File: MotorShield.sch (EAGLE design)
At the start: 127 parts, among them IC1 OPA4340E, IC2 OPA4340E, IC3 74HCT125D, IC4 MCP3008SL, T1 FDN337N, T2 FDN337N, T3 FDN337N, T4 FDN337N, T5 FDN337N, T6 FDN337N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

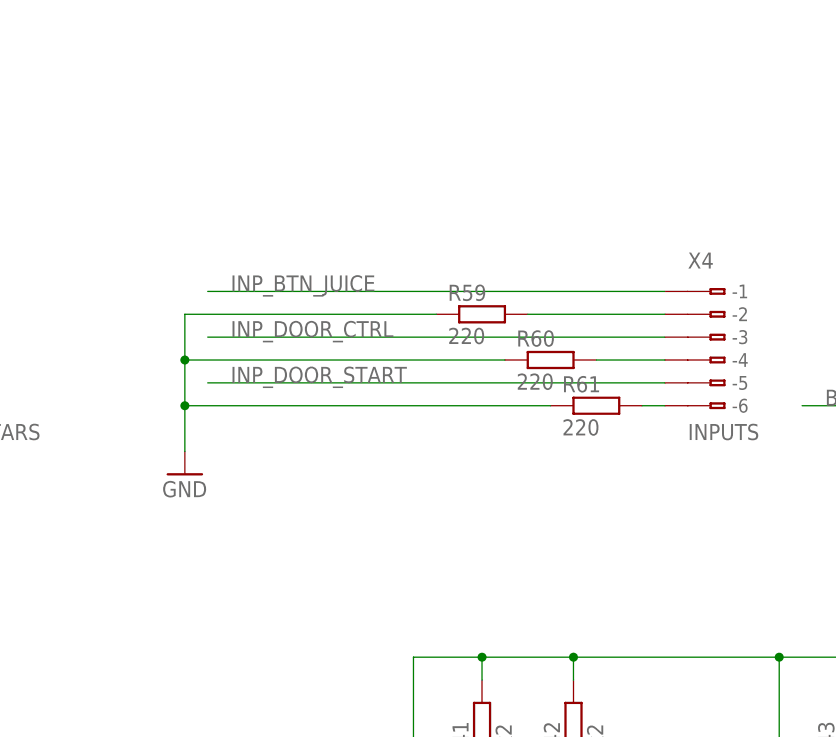
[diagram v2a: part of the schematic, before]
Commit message: debounced inputs fixes #20
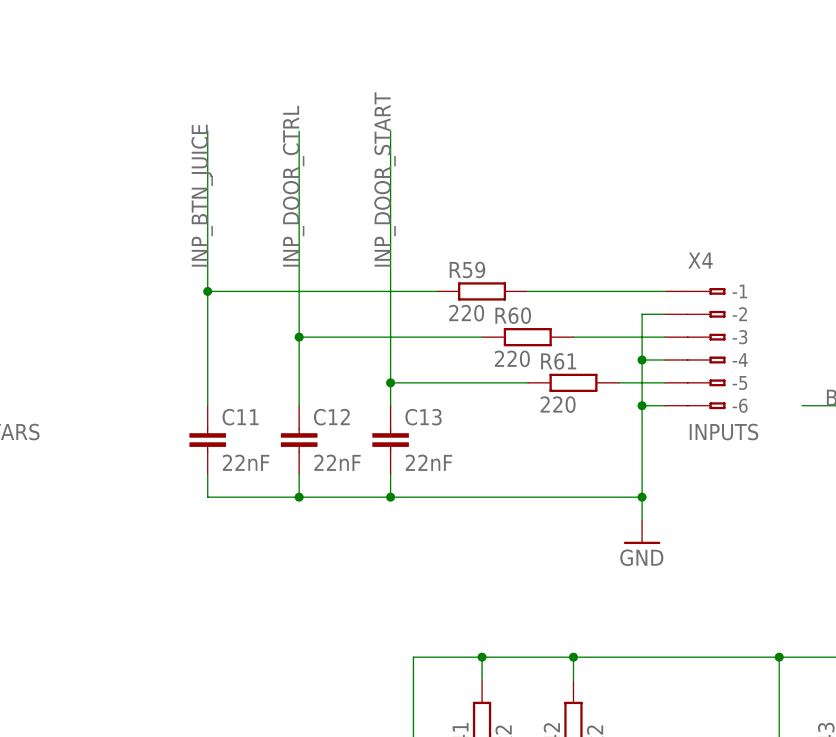
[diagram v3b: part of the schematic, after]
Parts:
- added C11, C12, C13: 22nF, rcl:C-EUC0805K
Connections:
- net GND: now also C11.2, C12.2, C13.2, X4.B-2, X4.B-4, X4.B-6; no longer R59.1, R60.1, R61.1
- net INP_BTN_JUICE: now also C11.1, R59.1; no longer X4.B-1
- net INP_DOOR_CTRL: now also C12.1, R60.1; no longer X4.B-3
- net INP_DOOR_START: now also C13.1, R61.1; no longer X4.B-5
- net N$33: now also X4.B-1; no longer X4.B-2
- net N$60: now also X4.B-3; no longer X4.B-4
- net N$61: now also X4.B-5; no longer X4.B-6
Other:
- moved on the sheet: R59, R60, R61
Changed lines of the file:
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@@
 <part name="R57" library="rcl" deviceset="R-EU_" device="R0805" value="2k2"/>
 <part name="LED18" library="led" deviceset="LED" device="CHIP-LED0805" value="yellow"/>
+<part name="C11" library="rcl" deviceset="C-EU" device="C0805K" value="22nF"/>
+<part name="C12" library="rcl" deviceset="C-EU" device="C0805K" value="22nF"/>
+<part name="C13" library="rcl" deviceset="C-EU" device="C0805K" value="22nF"/>
 </parts>
 <sheets>
@@
 <instance part="P+1" gate="1" x="175.26" y="226.06"/>
 <instance part="P+2" gate="1" x="487.68" y="172.72"/>
-<instance part="GND1" gate="1" x="83.82" y="177.8"/>
+<instance part="GND1" gate="1" x="134.62" y="170.18"/>
 <instance part="GND2" gate="1" x="411.48" y="53.34"/>
 <instance part="GND3" gate="1" x="175.26" y="167.64"/>
@@
 <instance part="T9" gate="A" x="175.26" y="187.96"/>
 <instance part="R62" gate="G$1" x="167.64" y="177.8" rot="R90"/>
-<instance part="R59" gate="G$1" x="116.84" y="195.58"/>
-<instance part="R60" gate="G$1" x="124.46" y="190.5"/>
-<instance part="R61" gate="G$1" x="129.54" y="185.42"/>
+<instance part="R59" gate="G$1" x="116.84" y="198.12"/>
+<instance part="R60" gate="G$1" x="121.92" y="193.04"/>
+<instance part="R61" gate="G$1" x="127" y="187.96"/>
 <instance part="LED17" gate="G$1" x="464.82" y="137.16"/>
 <instance part="R58" gate="G$1" x="464.82" y="154.94" rot="R90"/>
@@
 <instance part="R57" gate="G$1" x="167.64" y="213.36" rot="R90"/>
 <instance part="LED18" gate="G$1" x="167.64" y="203.2"/>
+<instance part="C11" gate="G$1" x="86.36" y="182.88"/>
+<instance part="C12" gate="G$1" x="96.52" y="182.88"/>
+<instance part="C13" gate="G$1" x="106.68" y="182.88"/>
 </instances>
 <busses>
@@
 </segment>
 <segment>
-<pinref part="GND1" gate="1" pin="GND"/>
-<wire x1="124.46" y1="185.42" x2="83.82" y2="185.42" width="0.1524" layer="91"/>
-<wire x1="83.82" y1="185.42" x2="83.82" y2="180.34" width="0.1524" layer="91"/>
-<wire x1="83.82" y1="185.42" x2="83.82" y2="190.5" width="0.1524" layer="91"/>
-<wire x1="83.82" y1="190.5" x2="119.38" y2="190.5" width="0.1524" layer="91"/>
-<junction x="83.82" y="185.42"/>
-<wire x1="83.82" y1="190.5" x2="83.82" y2="195.58" width="0.1524" layer="91"/>
-<wire x1="83.82" y1="195.58" x2="111.76" y2="195.58" width="0.1524" layer="91"/>
-<junction x="83.82" y="190.5"/>
-<pinref part="R61" gate="G$1" pin="1"/>
-<pinref part="R60" gate="G$1" pin="1"/>
-<pinref part="R59" gate="G$1" pin="1"/>
-</segment>
-<segment>
 <pinref part="GND3" gate="1" pin="GND"/>
 <wire x1="175.26" y1="170.18" x2="175.26" y2="172.72" width="0.1524" layer="91"/>
@@
 <wire x1="337.82" y1="10.16" x2="330.2" y2="10.16" width="0.1524" layer="91"/>
 <junction x="337.82" y="10.16"/>
+</segment>
+<segment>
+<pinref part="X4" gate="G$1" pin="B-6"/>
+<pinref part="GND1" gate="1" pin="GND"/>
+<wire x1="134.62" y1="185.42" x2="137.16" y2="185.42" width="0.1524" layer="91"/>
+<wire x1="134.62" y1="172.72" x2="134.62" y2="175.26" width="0.1524" layer="91"/>
+<junction x="134.62" y="185.42"/>
+<wire x1="134.62" y1="175.26" x2="134.62" y2="185.42" width="0.1524" layer="91"/>
+<wire x1="137.16" y1="190.5" x2="134.62" y2="190.5" width="0.1524" layer="91"/>
+<pinref part="X4" gate="G$1" pin="B-4"/>
+<wire x1="134.62" y1="185.42" x2="134.62" y2="190.5" width="0.1524" layer="91"/>
+<junction x="134.62" y="190.5"/>
+<pinref part="X4" gate="G$1" pin="B-2"/>
+<wire x1="134.62" y1="195.58" x2="137.16" y2="195.58" width="0.1524" layer="91"/>
+<wire x1="134.62" y1="190.5" x2="134.62" y2="195.58" width="0.1524" layer="91"/>
+<pinref part="C11" gate="G$1" pin="2"/>
+<wire x1="86.36" y1="177.8" x2="86.36" y2="175.26" width="0.1524" layer="91"/>
+<wire x1="86.36" y1="175.26" x2="96.52" y2="175.26" width="0.1524" layer="91"/>
+<junction x="134.62" y="175.26"/>
+<pinref part="C12" gate="G$1" pin="2"/>
+<wire x1="96.52" y1="175.26" x2="106.68" y2="175.26" width="0.1524" layer="91"/>
+<wire x1="106.68" y1="175.26" x2="134.62" y2="175.26" width="0.1524" layer="91"/>
+<wire x1="96.52" y1="177.8" x2="96.52" y2="175.26" width="0.1524" layer="91"/>
+<junction x="96.52" y="175.26"/>
+<pinref part="C13" gate="G$1" pin="2"/>
+<wire x1="106.68" y1="177.8" x2="106.68" y2="175.26" width="0.1524" layer="91"/>
+<junction x="106.68" y="175.26"/>
 </segment>
 </net>
@@
 <net name="INP_BTN_JUICE" class="0">
 <segment>
-<wire x1="137.16" y1="198.12" x2="86.36" y2="198.12" width="0.1524" layer="91"/>
-<label x="88.9" y="198.12" size="1.778" layer="95"/>
-<pinref part="X4" gate="G$1" pin="B-1"/>
+<label x="86.36" y="200.66" size="1.778" layer="95" rot="R90"/>
+<pinref part="R59" gate="G$1" pin="1"/>
+<wire x1="111.76" y1="198.12" x2="86.36" y2="198.12" width="0.1524" layer="91"/>
+<pinref part="C11" gate="G$1" pin="1"/>
+<wire x1="86.36" y1="185.42" x2="86.36" y2="198.12" width="0.1524" layer="91"/>
+<wire x1="86.36" y1="198.12" x2="86.36" y2="215.9" width="0.1524" layer="91"/>
+<junction x="86.36" y="198.12"/>
 </segment>
 <segment>
@@
 <net name="INP_DOOR_CTRL" class="0">
 <segment>
-<wire x1="86.36" y1="193.04" x2="137.16" y2="193.04" width="0.1524" layer="91"/>
-<label x="88.9" y="193.04" size="1.778" layer="95"/>
-<pinref part="X4" gate="G$1" pin="B-3"/>
+<label x="96.52" y="200.66" size="1.778" layer="95" rot="R90"/>
+<pinref part="R60" gate="G$1" pin="1"/>
+<pinref part="C12" gate="G$1" pin="1"/>
+<wire x1="96.52" y1="193.04" x2="116.84" y2="193.04" width="0.1524" layer="91"/>
+<wire x1="96.52" y1="185.42" x2="96.52" y2="193.04" width="0.1524" layer="91"/>
+<junction x="96.52" y="193.04"/>
+<wire x1="96.52" y1="193.04" x2="96.52" y2="215.9" width="0.1524" layer="91"/>
 </segment>
 <segment>
@@
 <net name="INP_DOOR_START" class="0">
 <segment>
-<wire x1="137.16" y1="187.96" x2="86.36" y2="187.96" width="0.1524" layer="91"/>
-<label x="88.9" y="187.96" size="1.778" layer="95"/>
-<pinref part="X4" gate="G$1" pin="B-5"/>
+<label x="106.68" y="200.66" size="1.778" layer="95" rot="R90"/>
+<pinref part="R61" gate="G$1" pin="1"/>
+<wire x1="121.92" y1="187.96" x2="106.68" y2="187.96" width="0.1524" layer="91"/>
+<pinref part="C13" gate="G$1" pin="1"/>
+<wire x1="106.68" y1="185.42" x2="106.68" y2="187.96" width="0.1524" layer="91"/>
+<junction x="106.68" y="187.96"/>
+<wire x1="106.68" y1="187.96" x2="106.68" y2="215.9" width="0.1524" layer="91"/>
 </segment>
 <segment>
@@
 </segment>
 </net>
-<net name="N$33" class="0">
-<segment>
-<pinref part="R59" gate="G$1" pin="2"/>
-<wire x1="121.92" y1="195.58" x2="137.16" y2="195.58" width="0.1524" layer="91"/>
-<pinref part="X4" gate="G$1" pin="B-2"/>
-</segment>
-</net>
-<net name="N$60" class="0">
-<segment>
-<pinref part="R60" gate="G$1" pin="2"/>
-<wire x1="137.16" y1="190.5" x2="129.54" y2="190.5" width="0.1524" layer="91"/>
-<pinref part="X4" gate="G$1" pin="B-4"/>
-</segment>
-</net>
-<net name="N$61" class="0">
-<segment>
-<pinref part="R61" gate="G$1" pin="2"/>
-<wire x1="134.62" y1="185.42" x2="137.16" y2="185.42" width="0.1524" layer="91"/>
-<pinref part="X4" gate="G$1" pin="B-6"/>
-</segment>
-</net>
 <net name="N$62" class="0">
 <segment>
@@
 </segment>
 </net>
+<net name="N$33" class="0">
+<segment>
+<pinref part="X4" gate="G$1" pin="B-1"/>
+<wire x1="137.16" y1="198.12" x2="121.92" y2="198.12" width="0.1524" layer="91"/>
+<pinref part="R59" gate="G$1" pin="2"/>
+</segment>
+</net>
+<net name="N$60" class="0">
+<segment>
+<pinref part="X4" gate="G$1" pin="B-3"/>
+<pinref part="R60" gate="G$1" pin="2"/>
+<wire x1="127" y1="193.04" x2="137.16" y2="193.04" width="0.1524" layer="91"/>
+</segment>
+</net>
+<net name="N$61" class="0">
+<segment>
+<pinref part="X4" gate="G$1" pin="B-5"/>
+<wire x1="137.16" y1="187.96" x2="132.08" y2="187.96" width="0.1524" layer="91"/>
+<pinref part="R61" gate="G$1" pin="2"/>
+</segment>
+</net>

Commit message: fixed footprint of L1 fixes #23
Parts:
- L1: value MPI4040 -> 1,5uH; device Spule:MPI4040 -> MPI4040:MPI4040R3-1R5-R
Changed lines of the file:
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@@
 <part name="R30" library="rcl" deviceset="R-EU_" device="R0805" value="1k"/>
 <part name="R16" library="rcl" deviceset="R-EU_" device="R0805" value="10k"/>
-<part name="L1" library="Spule" deviceset="MPI4040" device=""/>
 <part name="R7" library="rcl" deviceset="R-EU_" device="R0805" value="100m"/>
 <part name="C7" library="eagle-ltspice" deviceset="C" device="" value="10nF"/>
@@
 <part name="C12" library="rcl" deviceset="C-EU" device="C0805K" value="22nF"/>
 <part name="C13" library="rcl" deviceset="C-EU" device="C0805K" value="22nF"/>
+<part name="L1" library="MPI4040" deviceset="MPI4040R3-1R5-R" device="" value="1,5uH"/>
 </parts>
 <sheets>
@@
 <instance part="R30" gate="G$1" x="282" y="-85.2" rot="R90"/>
 <instance part="R16" gate="G$1" x="99.06" y="71.12" rot="R90"/>
-<instance part="L1" gate="G$1" x="495.3" y="162.56" rot="R270"/>
 <instance part="R7" gate="G$1" x="149.86" y="71.12" rot="R90"/>
 <instance part="C7" gate="G$1" x="167.64" y="71.12"/>
@@
 <instance part="C12" gate="G$1" x="96.52" y="182.88"/>
 <instance part="C13" gate="G$1" x="106.68" y="182.88"/>
+<instance part="L1" gate="G$1" x="502.92" y="162.56" rot="R180"/>
 </instances>
 <busses>
@@
 <pinref part="X1" gate="-1" pin="1"/>
 <wire x1="513.08" y1="142.24" x2="515.62" y2="142.24" width="0.1524" layer="91"/>
+<wire x1="515.62" y1="142.24" x2="515.62" y2="162.56" width="0.1524" layer="91"/>
 <pinref part="L1" gate="G$1" pin="P$1"/>
-<wire x1="515.62" y1="142.24" x2="515.62" y2="162.56" width="0.1524" layer="91"/>
-<wire x1="515.62" y1="162.56" x2="500.38" y2="162.56" width="0.1524" layer="91"/>
+<wire x1="508" y1="162.56" x2="515.62" y2="162.56" width="0.1524" layer="91"/>
 </segment>
 </net>
@@
 <segment>
 <pinref part="P+2" gate="1" pin="+24V"/>
-<pinref part="L1" gate="G$1" pin="P$2"/>
-<wire x1="490.22" y1="162.56" x2="487.68" y2="162.56" width="0.1524" layer="91"/>
 <junction x="487.68" y="162.56"/>
 <wire x1="487.68" y1="162.56" x2="487.68" y2="170.18" width="0.1524" layer="91"/>
@@
 <wire x1="464.82" y1="160.02" x2="464.82" y2="162.56" width="0.1524" layer="91"/>
 <wire x1="464.82" y1="162.56" x2="487.68" y2="162.56" width="0.1524" layer="91"/>
-</segment>
-<segment>
+<pinref part="L1" gate="G$1" pin="P$2"/>
+<wire x1="497.84" y1="162.56" x2="487.68" y2="162.56" width="0.1524" layer="91"/>
+</segment>
+<segment>
